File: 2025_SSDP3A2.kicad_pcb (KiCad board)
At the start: 4 copper layers, 58.4 x 28.8 mm, 67 parts, among them J1 SolderPad, J2 SolderPad, J3 SolderPad, J4 SolderPad, J5 SolderPad, J6 SolderPad, J7 SolderPad_01x02, J8 SolderPad_1x03, Q1 IAUZ30N10S5L240, Q2 BSZ096N10LS5, U1 LM5146RGYR

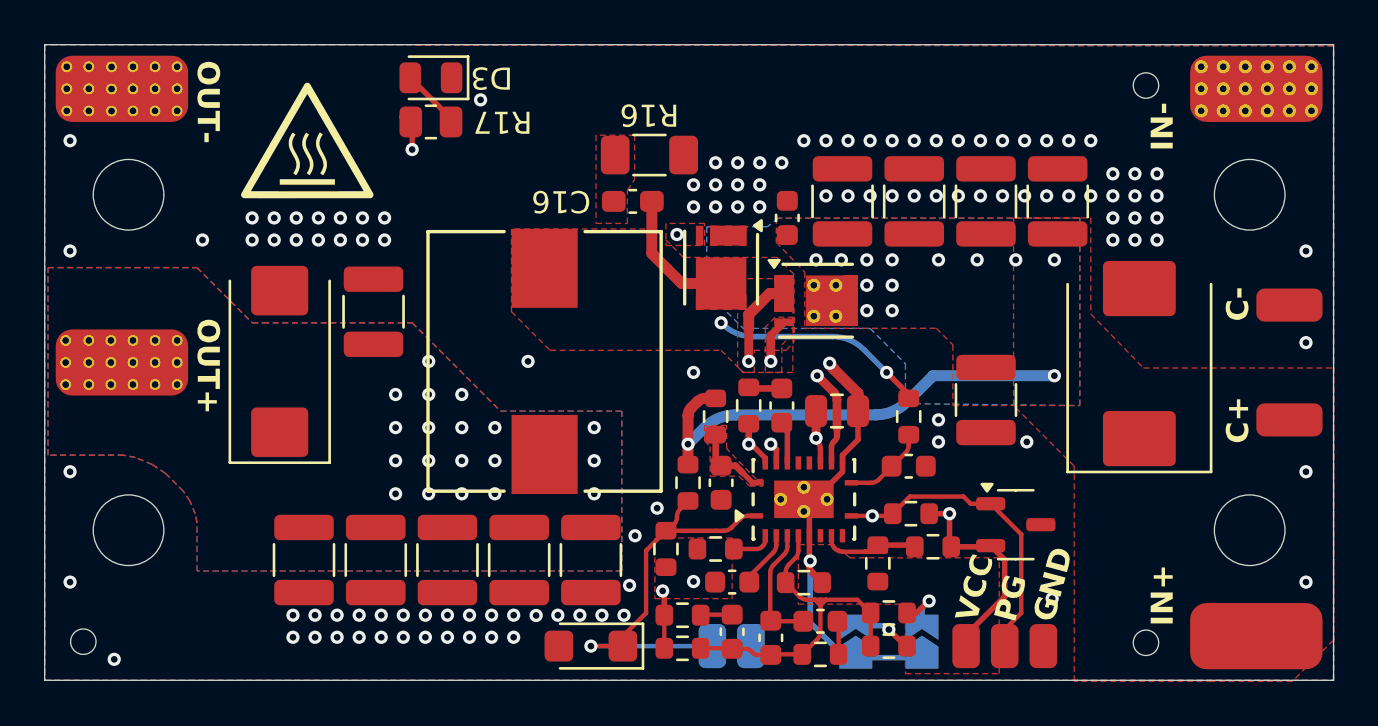
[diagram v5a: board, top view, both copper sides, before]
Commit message: Changed parts for LCSC availability, added silkscreen markings
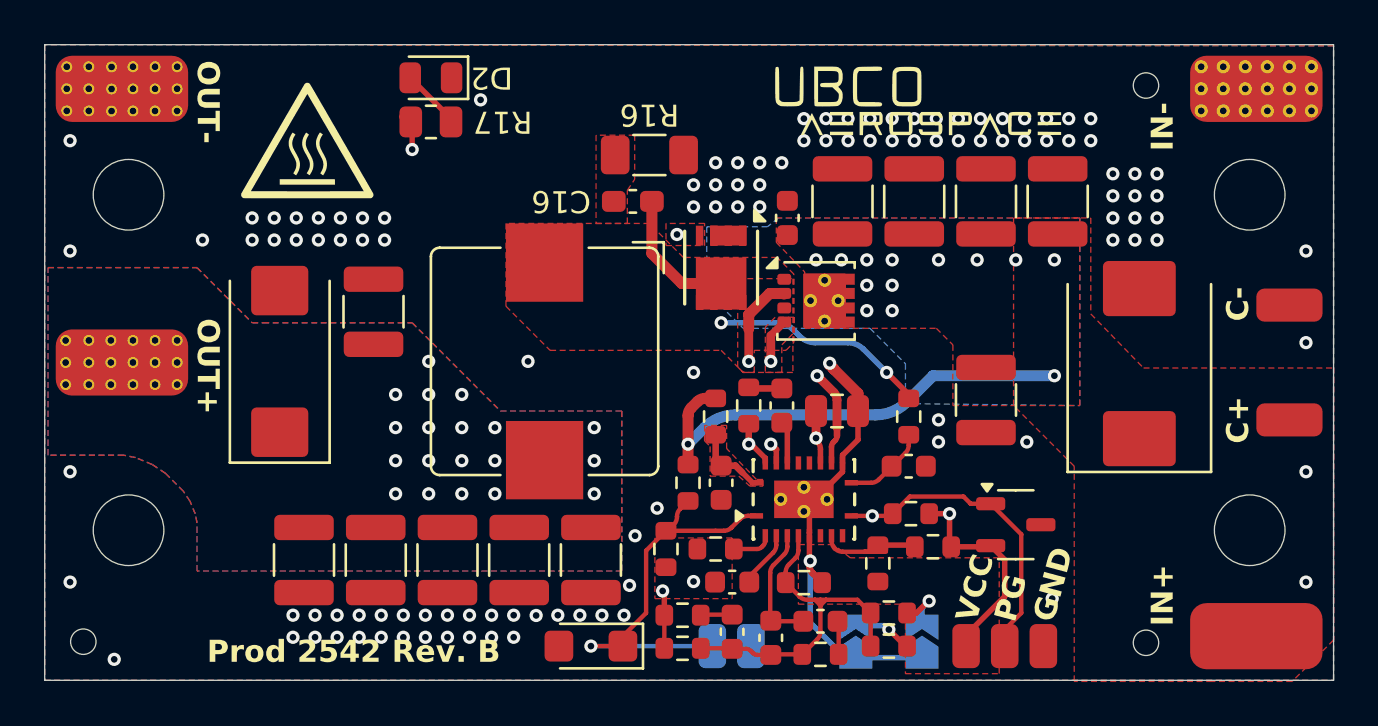
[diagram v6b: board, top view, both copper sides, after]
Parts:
- added G***: LOGO, LOGO, F.Cu at (159.7, 102.5)
- added G***: LOGO, LOGO, B.Cu at (147.8, 110.5)
- added G***: LOGO, LOGO, B.Cu at (161.8, 107.2)
- C12: value 3.3nF -> 4.7nF
- C13: value 47pF -> 68pF
- D3: renamed from D4; value SMF58A -> 60V
- L1: footprint PA4342-472NLT:IND_PA4342_PUL-M -> Inductor_SMD:L_Bourns_SRP1038C_10.0x10.0mm
- Q1: value IAUZ30N10S5L240 -> CSD19537Q3; footprint TSDSON-8:PG-TSDSON-8-26_TV -> Package_SON:VSON-8_3.3x3.3mm_P0.65mm_NexFET
- R10: value 12k -> 10k
- R8: value 220 -> 68
- moved G*** 5.65 mm to (146.5, 119.0)
- renumbered D3 to D2, D5 to D4
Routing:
- net PGND: vias 113 -> 114
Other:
- board text added: "INPUT: 20-60V⎓6A OUTPUT: 5.1-12V⎓8A"
- board text added: "JLCJLCJLCJLC"
- board text added: "Prod 2542 Rev. B"
- board text added: "Prod 2542 Rev. B Julian Joaquin"
- board text added: "SSD"
- board text added: "V3"
- board text removed: "INPUT: 20-60V⎓4A OUTPUT: 5.1-12V⎓8A"

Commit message: Fixed manufacturing errors
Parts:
- Q1: value CSD19537Q3 -> CSD19537Q3T
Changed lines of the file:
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@@
 			)
 		)
-		(property "FT Rotation Offset" "0"
+		(property "FT Rotation Offset" "-90"
 			(at 0 0 270)
 			(unlocked yes)
@@
 			)
 		)
-		(property "Value" "CSD19537Q3"
+		(property "Value" "CSD19537Q3T"
 			(at 0 2.8 0)
 			(layer "F.Fab")
@@
 			)
 		)
-		(property "Description" "CSD19537Q3"
+		(property "Description" "CSD19537Q3T"
 			(at 0 0 0)
 			(unlocked yes)
@@
 			)
 		)
-		(property "LCSC PN" "C478469"
+		(property "LCSC PN" "C134143"
 			(at 0 0 0)
 			(unlocked yes)
@@
 			)
 		)
-		(property "FT Rotation Offset" "0"
+		(property "FT Rotation Offset" "-90"
 			(at 0 0 90)
 			(unlocked yes)

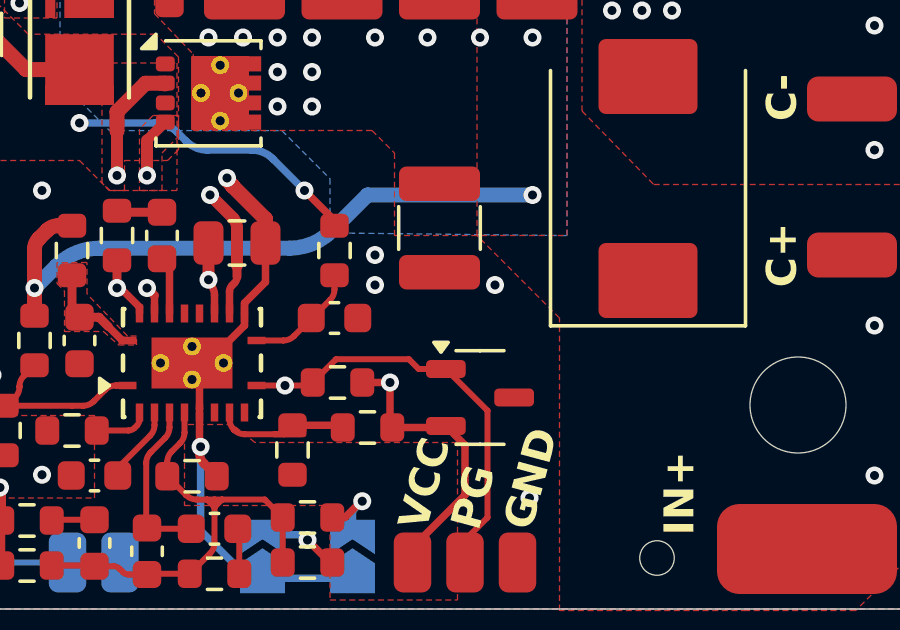
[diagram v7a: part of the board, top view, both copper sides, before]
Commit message: Changed part parameterization
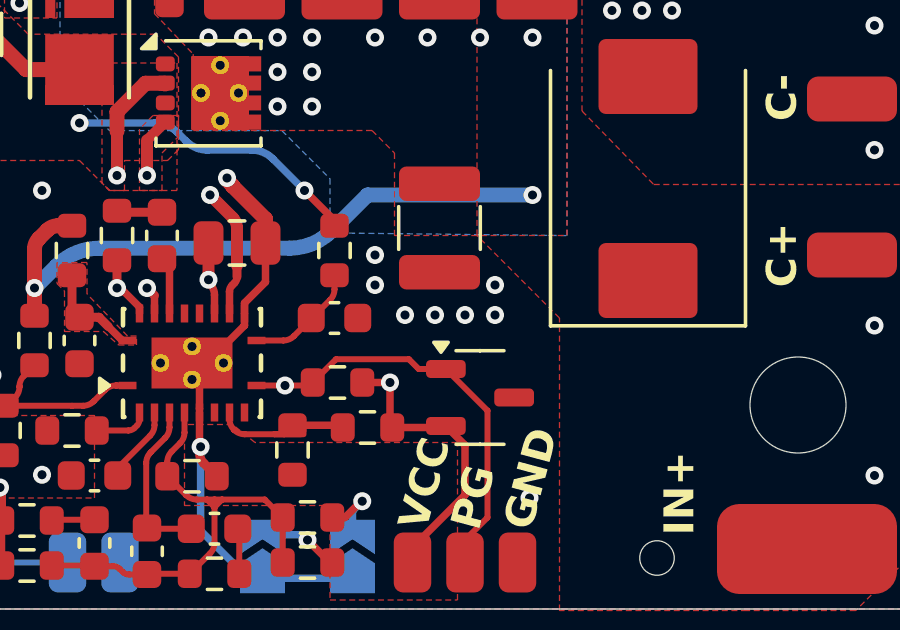
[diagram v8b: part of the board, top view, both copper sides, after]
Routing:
- net PGND: vias 114 -> 118
